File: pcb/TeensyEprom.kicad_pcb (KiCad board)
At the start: 2 copper layers, 65 x 28 mm, 0 parts

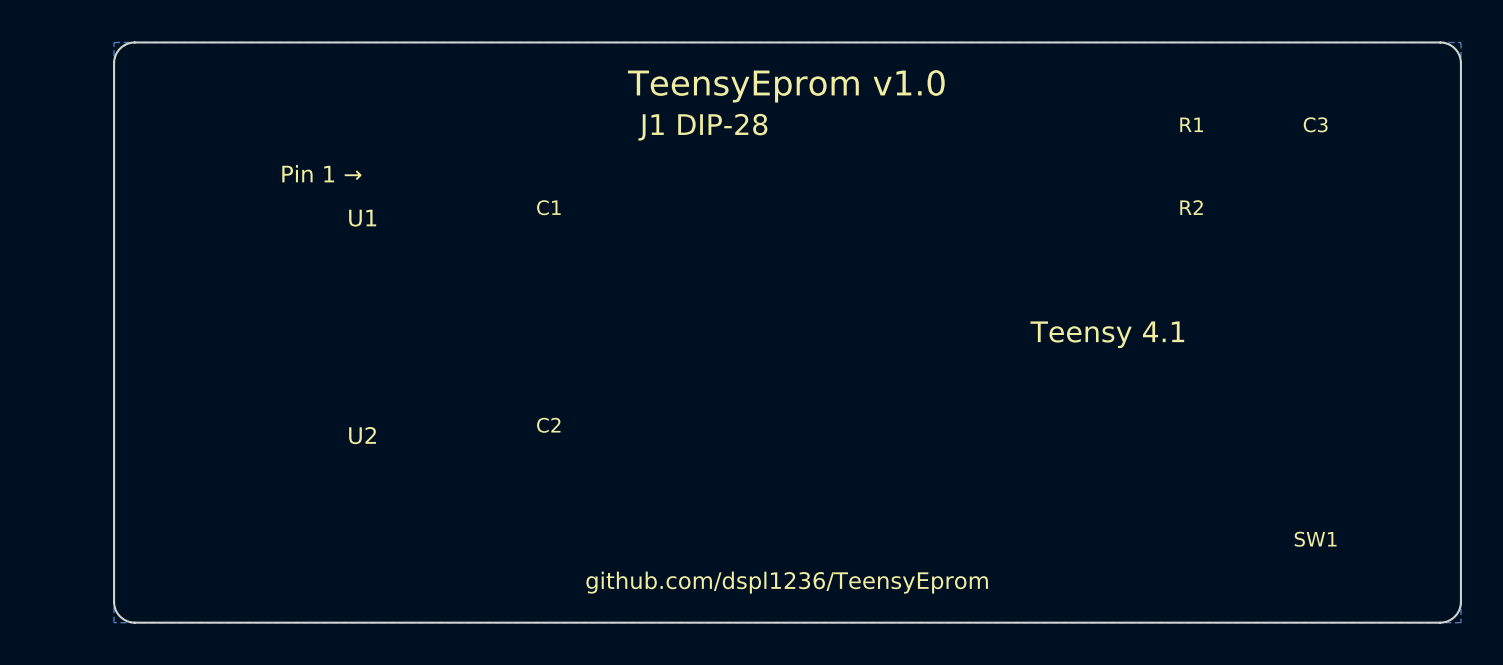
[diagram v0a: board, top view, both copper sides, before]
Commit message: fix: KiCad PCB syntax — remove comments, fix setup closure, add nets
PCB file had ;; comments (not valid in kicad_pcb format) and
malformed pcbplotparams nesting. Regenerated clean S-expressions.
Added net declarations (GND, +5V, +3V3, A0-A15, D0-D7, OE, CE, BTN).
Both files: balanced parens verified.
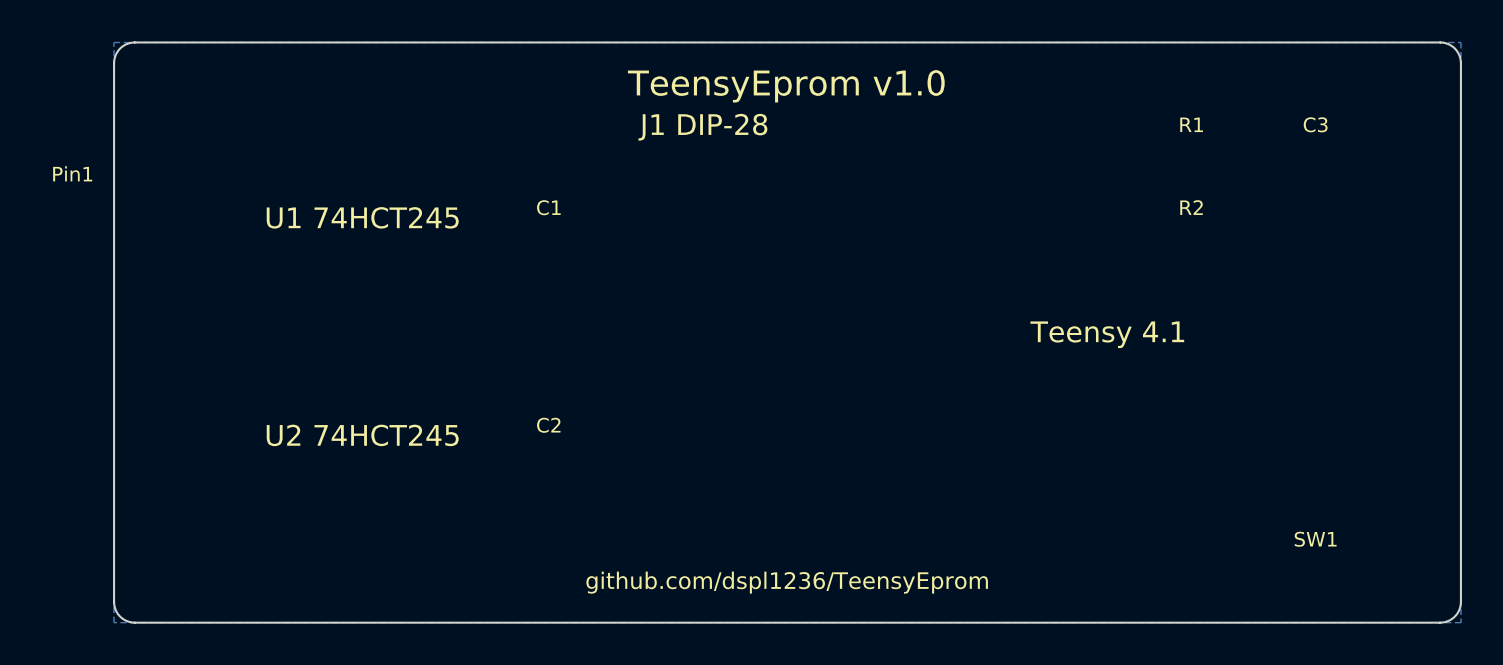
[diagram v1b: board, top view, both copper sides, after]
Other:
- board text added: "Pin1"
- board text added: "U1 74HCT245"
- board text added: "U2 74HCT245"
- board text removed: "Pin 1 →"
- board text removed: "U1"
- board text removed: "U2"
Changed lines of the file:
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@@
     (pad_to_mask_clearance 0.1)
     (allow_soldermask_bridges_in_footprints no)
-    (pcbplotparams (layerselection 0x00010fc_ffffffff) (plot_on_all_layers_selection 0x0000000_00000000)))
-  ;; Board outline: 65mm × 28mm, 1.0mm corner radius
+    (pcbplotparams
+      (layerselection 0x00010fc_ffffffff)
+      (plot_on_all_layers_selection 0x0000000_00000000)
+    )
+  )
+  (net 0 "")
+  (net 1 "GND")
+  (net 2 "+5V")
+  (net 3 "+3V3")
+  (net 4 "A0")
+  (net 5 "A1")
+  (net 6 "A2")
+  (net 7 "A3")
+  (net 8 "A4")
+  (net 9 "A5")
+  (net 10 "A6")
+  (net 11 "A7")
+  (net 12 "A8")
+  (net 13 "A9")
+  (net 14 "A10")
+  (net 15 "A11")
+  (net 16 "A12")
+  (net 17 "A13")
+  (net 18 "A14")
+  (net 19 "A15")
+  (net 20 "D0")
+  (net 21 "D1")
+  (net 22 "D2")
+  (net 23 "D3")
+  (net 24 "D4")
+  (net 25 "D5")
+  (net 26 "D6")
+  (net 27 "D7")
+  (net 28 "OE")
+  (net 29 "CE")
+  (net 30 "BTN")
   (gr_line (start 101.0 100) (end 164.0 100) (layer "Edge.Cuts") (width 0.1))
   (gr_line (start 165 101.0) (end 165 127.0) (layer "Edge.Cuts") (width 0.1))
@@
   (gr_text "github.com/dspl1236/TeensyEprom" (at 132.5 126) (layer "F.SilkS")
     (effects (font (size 0.8 0.8) (thickness 0.1))))
-  ;; J1: DIP-28 at (112, 114.0), pins extend through board and below
   (gr_text "J1 DIP-28" (at 128.5 104.0) (layer "F.SilkS")
-    (effects (font (size 1 1) (thickness 0.15))))
-  (gr_text "Pin 1 →" (at 110 106.38) (layer "F.SilkS")
-    (effects (font (size 0.8 0.8) (thickness 0.1))))
+    (effects (font (size 1.0 1.0) (thickness 0.1))))
+  (gr_text "Pin1" (at 98 106.38) (layer "F.SilkS")
+    (effects (font (size 0.7 0.7) (thickness 0.1))))
+  (gr_text "Teensy 4.1" (at 148 114.0) (layer "F.SilkS")
+    (effects (font (size 1.0 1.0) (thickness 0.1))))
+  (gr_text "U1 74HCT245" (at 112 108.5) (layer "F.SilkS")
+    (effects (font (size 1.0 1.0) (thickness 0.1))))
+  (gr_text "U2 74HCT245" (at 112 119.0) (layer "F.SilkS")
+    (effects (font (size 1.0 1.0) (thickness 0.1))))
+  (gr_text "R1" (at 152 104) (layer "F.SilkS")
+    (effects (font (size 0.7 0.7) (thickness 0.1))))
+  (gr_text "R2" (at 152 108) (layer "F.SilkS")
+    (effects (font (size 0.7 0.7) (thickness 0.1))))
+  (gr_text "C1" (at 121 108) (layer "F.SilkS")
+    (effects (font (size 0.7 0.7) (thickness 0.1))))
+  (gr_text "C2" (at 121 118.5) (layer "F.SilkS")
+    (effects (font (size 0.7 0.7) (thickness 0.1))))
+  (gr_text "C3" (at 158 104) (layer "F.SilkS")
+    (effects (font (size 0.7 0.7) (thickness 0.1))))
+  (gr_text "SW1" (at 158 124) (layer "F.SilkS")
+    (effects (font (size 0.7 0.7) (thickness 0.1))))
   (gr_circle (center 112.0 106.38) (end 112.5 106.38) (layer "Dwgs.User") (width 0.1))
   (gr_circle (center 112.0 121.62) (end 112.5 121.62) (layer "Dwgs.User") (width 0.1))
@@
   (gr_circle (center 145.02 106.38) (end 145.52 106.38) (layer "Dwgs.User") (width 0.1))
   (gr_circle (center 145.02 121.62) (end 145.52 121.62) (layer "Dwgs.User") (width 0.1))
-  ;; U0: Teensy 4.1 headers at (118, 114.0)
-  (gr_text "Teensy 4.1" (at 148 114.0) (layer "F.SilkS")
-    (effects (font (size 1 1) (thickness 0.15))))
   (gr_circle (center 118.0 106.38) (end 118.4 106.38) (layer "Dwgs.User") (width 0.1))
   (gr_circle (center 118.0 121.62) (end 118.4 121.62) (layer "Dwgs.User") (width 0.1))
@@
   (gr_circle (center 176.42000000000002 106.38) (end 176.82000000000002 106.38) (layer "Dwgs.User") (width 0.1))
   (gr_circle (center 176.42000000000002 121.62) (end 176.82000000000002 121.62) (layer "Dwgs.User") (width 0.1))
-  ;; U1: 74HCT245 SOIC-20 at (106, 105)
-  (gr_text "U1" (at 112 108.5) (layer "F.SilkS")
-    (effects (font (size 0.8 0.8) (thickness 0.1))))
   (gr_rect (start 106 105) (end 119 112.5) (layer "Dwgs.User") (width 0.15))
-  ;; U2: 74HCT245 SOIC-20 at (106, 115.5)
-  (gr_text "U2" (at 112 119.0) (layer "F.SilkS")
-    (effects (font (size 0.8 0.8) (thickness 0.1))))
   (gr_rect (start 106 115.5) (end 119 123.0) (layer "Dwgs.User") (width 0.15))
-  ;; Passives
-  (gr_text "R1" (at 152 104) (layer "F.SilkS")
-    (effects (font (size 0.7 0.7) (thickness 0.1))))
-  (gr_text "R2" (at 152 108) (layer "F.SilkS")
-    (effects (font (size 0.7 0.7) (thickness 0.1))))
-  (gr_text "C1" (at 121 108) (layer "F.SilkS")
-    (effects (font (size 0.7 0.7) (thickness 0.1))))
-  (gr_text "C2" (at 121 118.5) (layer "F.SilkS")
-    (effects (font (size 0.7 0.7) (thickness 0.1))))
-  (gr_text "C3" (at 158 104) (layer "F.SilkS")
-    (effects (font (size 0.7 0.7) (thickness 0.1))))
-  (gr_text "SW1" (at 158 124) (layer "F.SilkS")
-    (effects (font (size 0.7 0.7) (thickness 0.1))))
-  ;; Ground pour — back copper
-  (zone (net 0) (net_name "GND") (layer "B.Cu")
+  (zone (net 1) (net_name "GND") (layer "B.Cu")
     (hatch edge 0.5)
     (connect_pads (clearance 0.3))
